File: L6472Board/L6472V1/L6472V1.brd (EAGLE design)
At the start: 76.2 x 76.2 mm, 36 parts

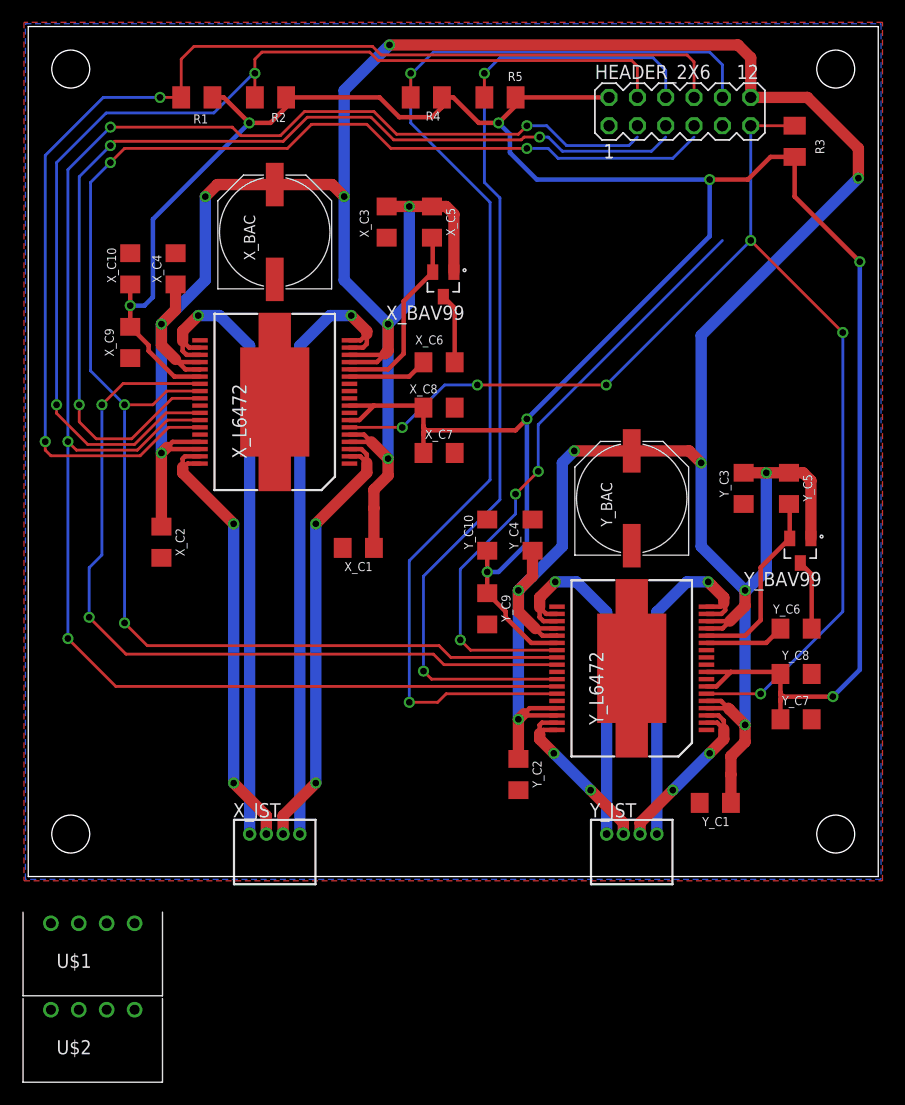
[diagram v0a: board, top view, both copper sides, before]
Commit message: Revision of Motorcontroller Board
Footprints for the stepper motor connectors and BACs were replaced.
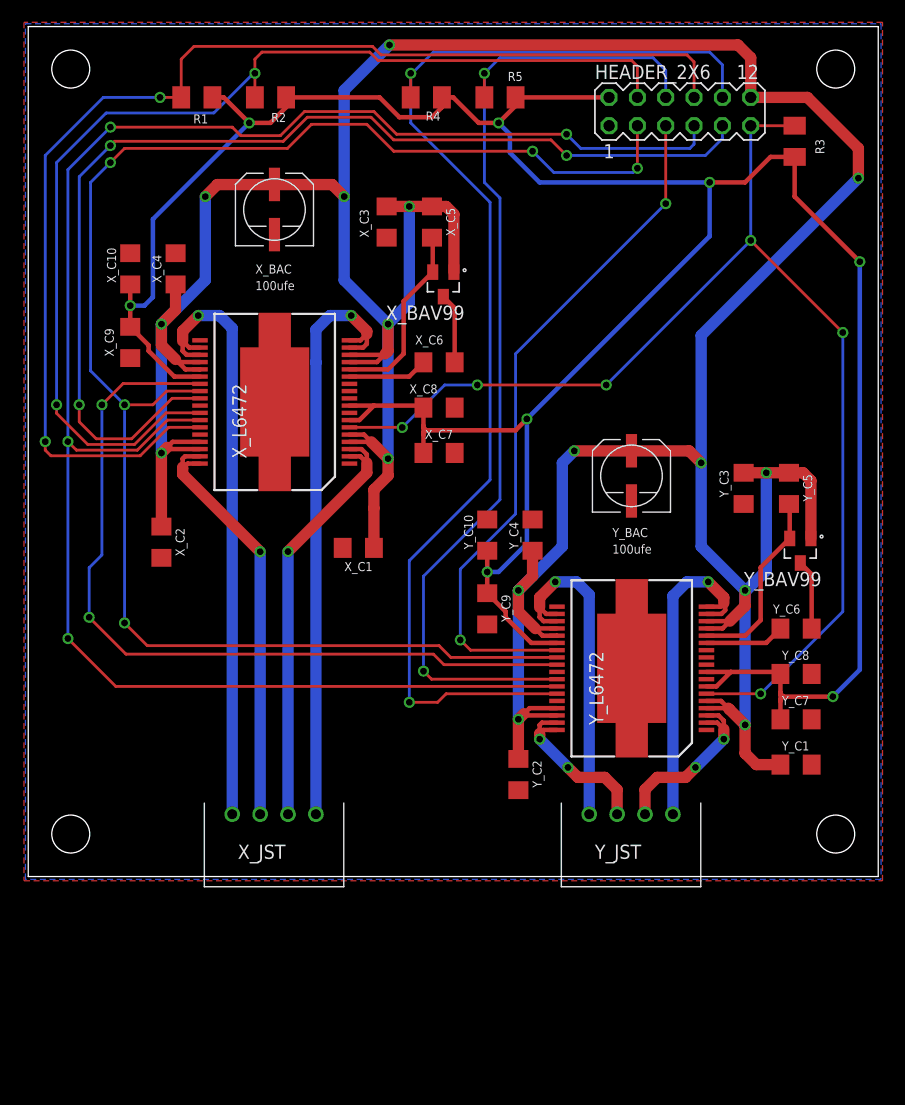
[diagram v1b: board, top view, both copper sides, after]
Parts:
- removed U$1, U$2: JST, L6472LIB:JST-4
- X_BAC, Y_BAC: device L6472LIB:CAPAE1030X1200 -> L6472LIB:EEE1AA101WR
- X_JST, Y_JST: value S4B-ZR -> JST; device con-jst:S4B-ZR -> L6472LIB:JST-4
- moved Y_C1 8.01 mm to (68.8, 10.0), turned to 0 degrees
- moved X_JST 4.20 mm to (18.3, 5.59)
- moved Y_JST 4.20 mm to (50.3, 5.59)
- moved X_BAC 1.70 mm to (20.6, 58.5), turned to 0 degrees
- moved Y_BAC 1.70 mm to (52.6, 34.7), turned to 0 degrees
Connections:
- net GND: now also X_BAC.CATHODE, Y_BAC.CATHODE; no longer X_BAC.-, Y_BAC.-
- net VS: now also X_BAC.ANODE, Y_BAC.ANODE; no longer X_BAC.+, Y_BAC.+
- net X_1A: now also X_JST.P2; no longer U$1.P2, X_JST.3
- net X_1B: now also X_JST.P3; no longer U$1.P3, X_JST.4
- net X_2A: now also X_JST.P1; no longer U$1.P1, X_JST.2
- net X_2B: now also X_JST.P0; no longer U$1.P0, X_JST.1
- net Y_1A: now also Y_JST.P2; no longer U$2.P2, Y_JST.3
- net Y_1B: now also Y_JST.P3; no longer U$2.P3, Y_JST.4
- net Y_2A: now also Y_JST.P1; no longer U$2.P1, Y_JST.2
- net Y_2B: now also Y_JST.P0; no longer U$2.P0, Y_JST.1
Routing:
- net MISO: track 54.6 -> 62.8 mm, vias 3 -> 2
- net MOSI: track 91.7 -> 98.0 mm
- net CS: track 157.0 -> 163.0 mm
- net Y_2B: track 32.8 -> 30.4 mm
- net X_2B: track 56.8 -> 54.3 mm
- net Y_1B: track 32.8 -> 30.4 mm
- net X_1B: track 56.1 -> 53.7 mm
- net X_2A: track 40.1 -> 38.1 mm, vias 2 -> 1
- net X_1A: track 40.7 -> 38.7 mm, vias 2 -> 1
- net CLK: track 146.4 -> 145.0 mm, vias 4 -> 5
- net VS: track 364.9 -> 363.5 mm
- net Y_2A: track 16.3 -> 15.7 mm

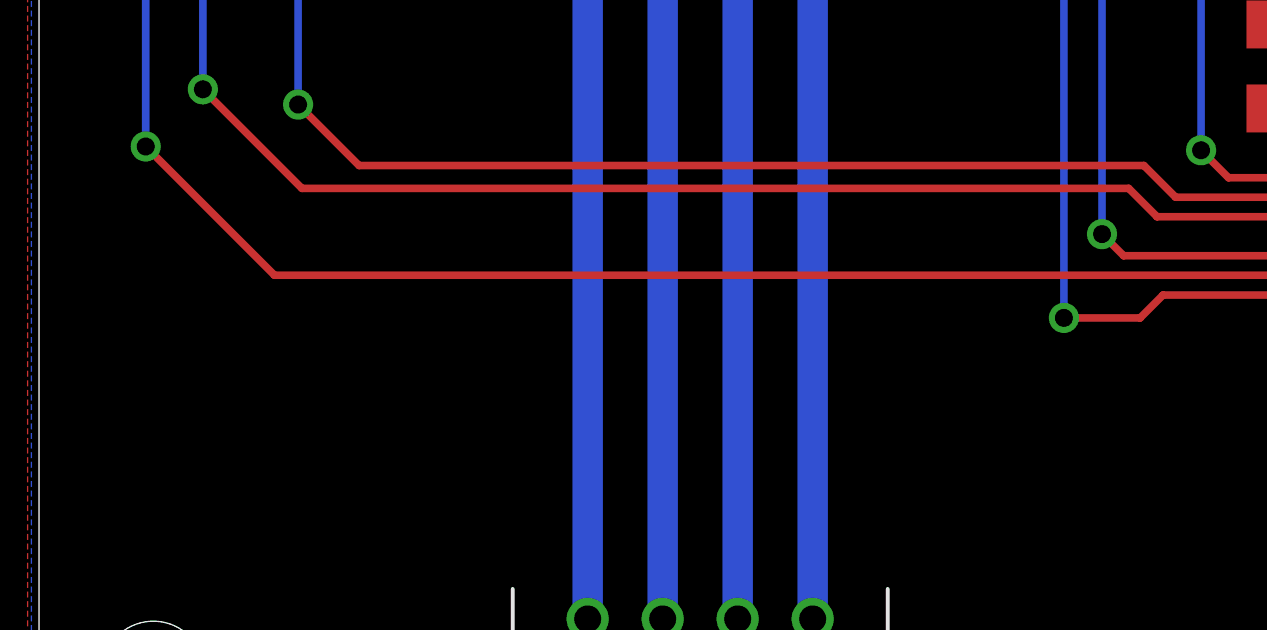
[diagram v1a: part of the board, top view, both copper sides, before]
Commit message: Updates to Laser and Power Board
Updated emergency shutoff button footprint, led button voltage changed
to 5v, and switched level shifter to 74LVC1T45.
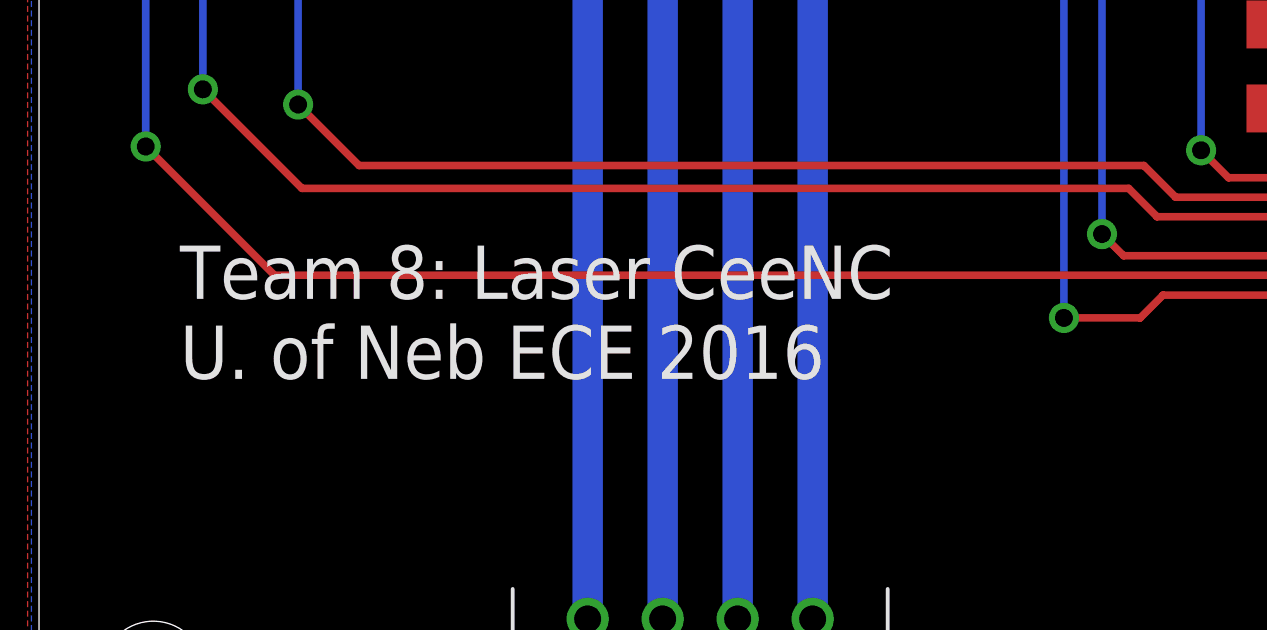
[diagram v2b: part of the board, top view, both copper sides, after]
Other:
- board text added: "Team 8: Laser CeeNC U. of Neb ECE 2016"
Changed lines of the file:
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@@
 <hole x="72.39" y="3.81" drill="3.4036"/>
 <hole x="3.81" y="3.81" drill="3.4036"/>
+<text x="4.699" y="13.589" size="1.778" layer="21">Team 8: Laser CeeNC
+U. of Neb ECE 2016</text>
 </plain>
 <attributes>
@@
 </board>
 </drawing>
+<compatibility>
+<note version="6.3" minversion="6.2.2" severity="warning">
+Since Version 6.2.2 text objects can contain more than one line,
+which will not be processed correctly with this version.
+</note>
+</compatibility>
 </eagle>

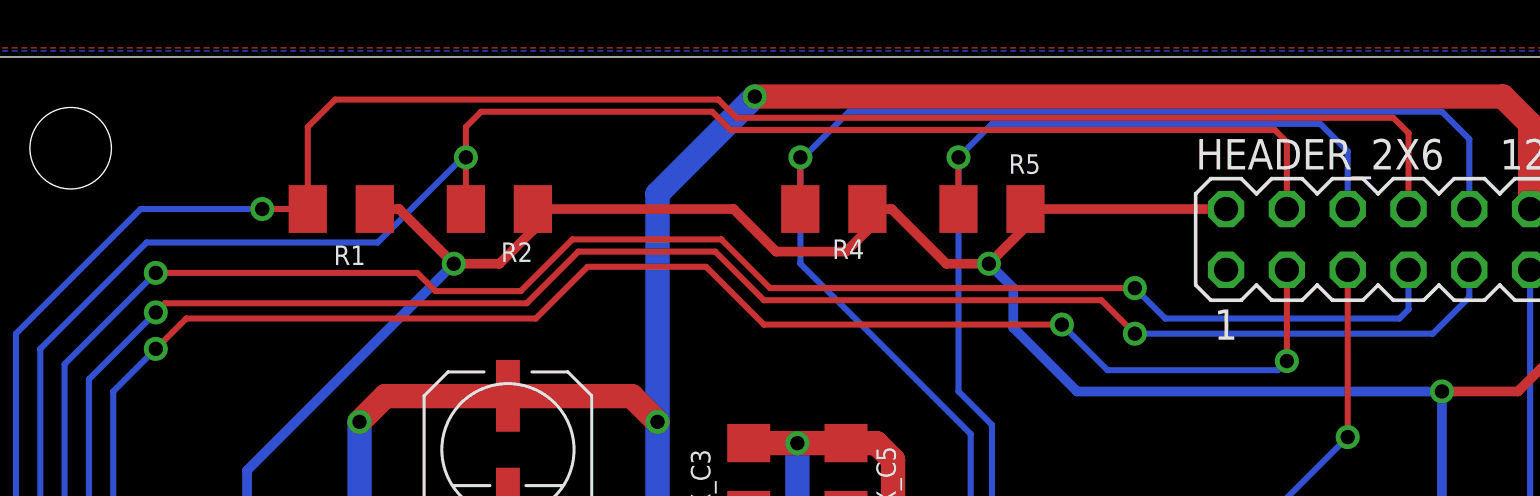
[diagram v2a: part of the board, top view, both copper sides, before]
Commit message: Final Revisions to PCBs and Schematics
Final revisions made to the PCBs and schematics. This is the version
which will be sent out to the board house for round two.
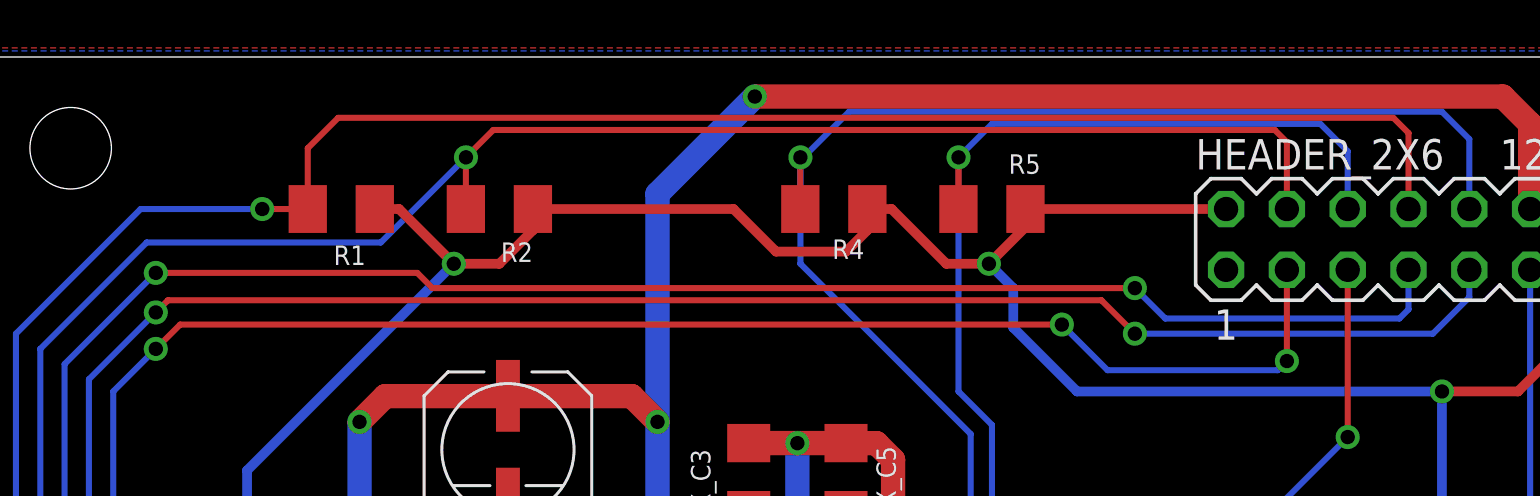
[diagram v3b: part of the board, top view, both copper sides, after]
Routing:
- net CLK: track 145.0 -> 143.0 mm
- net CS: track 163.0 -> 161.2 mm
- net MOSI: track 98.0 -> 96.3 mm
- net X_BUSY: track 100.1 -> 98.7 mm
- net X_FLAG: track 109.5 -> 108.4 mm
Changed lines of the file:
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@@
 <layer number="26" name="bNames" color="7" fill="1" visible="yes" active="yes"/>
 <layer number="27" name="tValues" color="7" fill="1" visible="no" active="yes"/>
-<layer number="28" name="bValues" color="7" fill="1" visible="yes" active="yes"/>
+<layer number="28" name="bValues" color="7" fill="1" visible="no" active="yes"/>
 <layer number="29" name="tStop" color="7" fill="3" visible="yes" active="yes"/>
 <layer number="30" name="bStop" color="7" fill="6" visible="yes" active="yes"/>
@@
 <via x="11.811" y="69.85" extent="1-16" drill="0.6"/>
 <wire x1="11.811" y1="69.85" x2="13.713" y2="69.85" width="0.254" layer="1"/>
-<wire x1="13.713" y1="69.85" x2="13.713" y2="73.276" width="0.254" layer="1"/>
-<wire x1="13.713" y1="73.276" x2="14.859" y2="74.422" width="0.254" layer="1"/>
-<wire x1="14.859" y1="74.422" x2="30.861" y2="74.422" width="0.254" layer="1"/>
-<wire x1="30.861" y1="74.422" x2="31.623" y2="73.66" width="0.254" layer="1"/>
-<wire x1="31.623" y1="73.66" x2="59.055" y2="73.66" width="0.254" layer="1"/>
+<wire x1="13.713" y1="69.85" x2="13.713" y2="72.39" width="0.254" layer="1"/>
+<wire x1="14.983" y1="73.66" x2="59.055" y2="73.66" width="0.254" layer="1"/>
 <wire x1="59.055" y1="73.66" x2="59.69" y2="73.025" width="0.254" layer="1"/>
 <wire x1="59.69" y1="73.025" x2="59.69" y2="69.85" width="0.254" layer="1"/>
@@
 <wire x1="1.524" y1="38.227" x2="1.524" y2="38.989" width="0.254" layer="1"/>
 <wire x1="2.032" y1="37.719" x2="10.033" y2="37.719" width="0.254" layer="1"/>
+<wire x1="14.983" y1="73.66" x2="13.713" y2="72.39" width="0.254" layer="1"/>
 </signal>
 <signal name="X_BUSY">
@@
 <contactref element="HEADER_2X6" pad="4"/>
 <contactref element="R2" pad="2"/>
-<wire x1="20.317" y1="73.276" x2="20.955" y2="73.914" width="0.254" layer="1"/>
-<wire x1="20.955" y1="73.914" x2="30.607" y2="73.914" width="0.254" layer="1"/>
-<wire x1="30.607" y1="73.914" x2="31.369" y2="73.152" width="0.254" layer="1"/>
-<wire x1="31.369" y1="73.152" x2="54.102" y2="73.152" width="0.254" layer="1"/>
+<wire x1="21.463" y1="73.152" x2="54.102" y2="73.152" width="0.254" layer="1"/>
 <wire x1="54.102" y1="73.152" x2="54.61" y2="72.644" width="0.254" layer="1"/>
 <wire x1="54.61" y1="72.644" x2="54.61" y2="69.85" width="0.254" layer="1"/>
@@
 <via x="2.54" y="42.291" extent="1-16" drill="0.6"/>
 <wire x1="2.54" y1="42.291" x2="2.54" y2="64.008" width="0.254" layer="16"/>
-<wire x1="6.985" y1="68.453" x2="16.637" y2="68.453" width="0.254" layer="16"/>
+<wire x1="6.985" y1="68.453" x2="16.764" y2="68.453" width="0.254" layer="16"/>
 <wire x1="2.54" y1="64.008" x2="6.985" y2="68.453" width="0.254" layer="16"/>
 <wire x1="20.317" y1="69.85" x2="20.317" y2="72.006" width="0.254" layer="1"/>
 <wire x1="20.317" y1="72.006" x2="20.32" y2="72.009" width="0.254" layer="1"/>
 <via x="20.32" y="72.009" extent="1-16" drill="0.6"/>
-<wire x1="20.32" y1="72.009" x2="20.193" y2="72.009" width="0.254" layer="16"/>
-<wire x1="20.193" y1="72.009" x2="16.637" y2="68.453" width="0.254" layer="16"/>
-<wire x1="20.317" y1="72.006" x2="20.317" y2="73.276" width="0.254" layer="1"/>
 <wire x1="5.334" y1="38.735" x2="2.54" y2="41.529" width="0.254" layer="1"/>
 <wire x1="2.54" y1="41.529" x2="2.54" y2="42.291" width="0.254" layer="1"/>
 <wire x1="5.334" y1="38.735" x2="9.525" y2="38.735" width="0.254" layer="1"/>
+<wire x1="21.463" y1="73.152" x2="20.32" y2="72.009" width="0.254" layer="1"/>
+<wire x1="16.764" y1="68.453" x2="20.32" y2="72.009" width="0.254" layer="16"/>
 </signal>
 <signal name="STBY">
@@
 <wire x1="4.572" y1="62.738" x2="7.366" y2="65.532" width="0.254" layer="16"/>
 <via x="7.366" y="65.532" extent="1-16" drill="0.6"/>
-<wire x1="22.86" y1="65.913" x2="25.019" y2="68.072" width="0.254" layer="1"/>
-<wire x1="25.019" y1="68.072" x2="30.734" y2="68.072" width="0.254" layer="1"/>
-<wire x1="30.734" y1="68.072" x2="32.766" y2="66.04" width="0.254" layer="1"/>
-<wire x1="22.86" y1="65.913" x2="7.747" y2="65.913" width="0.254" layer="1"/>
-<wire x1="7.747" y1="65.913" x2="7.366" y2="65.532" width="0.254" layer="1"/>
 <wire x1="6.096" y1="39.243" x2="4.572" y2="40.767" width="0.254" layer="1"/>
 <wire x1="4.572" y1="40.767" x2="4.572" y2="42.291" width="0.254" layer="1"/>
 <wire x1="9.271" y1="39.243" x2="6.096" y2="39.243" width="0.254" layer="1"/>
-<wire x1="46.863" y1="66.04" x2="32.766" y2="66.04" width="0.254" layer="1"/>
 <contactref element="HEADER_2X6" pad="9"/>
 <wire x1="62.23" y1="67.31" x2="62.23" y2="66.167" width="0.254" layer="16"/>
@@
 <wire x1="60.706" y1="64.643" x2="62.23" y2="66.167" width="0.254" layer="16"/>
 <wire x1="48.26" y1="64.643" x2="46.863" y2="66.04" width="0.254" layer="1"/>
+<wire x1="46.863" y1="66.04" x2="7.874" y2="66.04" width="0.254" layer="1"/>
+<wire x1="7.874" y1="66.04" x2="7.366" y2="65.532" width="0.254" layer="1"/>
 </signal>
 <signal name="DAISY">
@@
 <via x="7.366" y="64.008" extent="1-16" drill="0.6"/>
 <wire x1="5.588" y1="62.23" x2="7.366" y2="64.008" width="0.254" layer="16"/>
-<wire x1="23.241" y1="65.278" x2="25.4" y2="67.437" width="0.254" layer="1"/>
-<wire x1="25.4" y1="67.437" x2="30.353" y2="67.437" width="0.254" layer="1"/>
-<wire x1="30.353" y1="67.437" x2="32.766" y2="65.024" width="0.254" layer="1"/>
-<wire x1="23.241" y1="65.278" x2="8.636" y2="65.278" width="0.254" layer="1"/>
-<wire x1="8.636" y1="65.278" x2="7.366" y2="64.008" width="0.254" layer="1"/>
 <via x="8.636" y="42.291" extent="1-16" drill="0.6"/>
 <wire x1="15.398" y1="43.52" x2="12.405" y2="43.52" width="0.254" layer="1"/>
@@
 <wire x1="54.61" y1="63.5" x2="54.229" y2="63.119" width="0.254" layer="16"/>
 <wire x1="54.229" y1="63.119" x2="47.117" y2="63.119" width="0.254" layer="16"/>
-<wire x1="32.766" y1="65.024" x2="45.212" y2="65.024" width="0.254" layer="1"/>
 <via x="45.212" y="65.024" extent="1-16" drill="0.6"/>
 <wire x1="45.212" y1="65.024" x2="47.117" y2="63.119" width="0.254" layer="16"/>
+<wire x1="45.212" y1="65.024" x2="8.382" y2="65.024" width="0.254" layer="1"/>
+<wire x1="8.382" y1="65.024" x2="7.366" y2="64.008" width="0.254" layer="1"/>
 </signal>
 <signal name="CS">
@@
 <wire x1="3.556" y1="63.373" x2="7.366" y2="67.183" width="0.254" layer="16"/>
 <via x="7.366" y="67.183" extent="1-16" drill="0.6"/>
-<wire x1="7.366" y1="67.183" x2="18.288" y2="67.183" width="0.254" layer="1"/>
-<wire x1="18.288" y1="67.183" x2="19.05" y2="66.421" width="0.254" layer="1"/>
-<wire x1="19.05" y1="66.421" x2="22.606" y2="66.421" width="0.254" layer="1"/>
-<wire x1="22.606" y1="66.421" x2="24.765" y2="68.58" width="0.254" layer="1"/>
-<wire x1="24.765" y1="68.58" x2="30.988" y2="68.58" width="0.254" layer="1"/>
-<wire x1="30.988" y1="68.58" x2="33.02" y2="66.548" width="0.254" layer="1"/>
 <wire x1="7.848" y1="17.044" x2="3.556" y2="21.336" width="0.254" layer="1"/>
 <wire x1="3.556" y1="21.336" x2="3.556" y2="38.989" width="0.254" layer="16"/>
@@
 <wire x1="9.779" y1="38.227" x2="4.318" y2="38.227" width="0.254" layer="1"/>
 <wire x1="7.848" y1="17.044" x2="47.402" y2="17.044" width="0.254" layer="1"/>
-<wire x1="33.02" y1="66.548" x2="48.26" y2="66.548" width="0.254" layer="1"/>
+<wire x1="18.923" y1="66.548" x2="48.26" y2="66.548" width="0.254" layer="1"/>
 <contactref element="HEADER_2X6" pad="7"/>
 <via x="48.26" y="66.548" extent="1-16" drill="0.6"/>
@@
 <wire x1="59.309" y1="65.278" x2="59.69" y2="65.659" width="0.254" layer="16"/>
 <wire x1="59.69" y1="65.659" x2="59.69" y2="67.31" width="0.254" layer="16"/>
+<wire x1="18.923" y1="66.548" x2="18.288" y2="67.183" width="0.254" layer="1"/>
+<wire x1="18.288" y1="67.183" x2="7.366" y2="67.183" width="0.254" layer="1"/>
 </signal>
 <signal name="Y_FLAG">
